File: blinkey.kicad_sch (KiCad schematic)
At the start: 34 parts, among them SW1 SW_DIP_x04

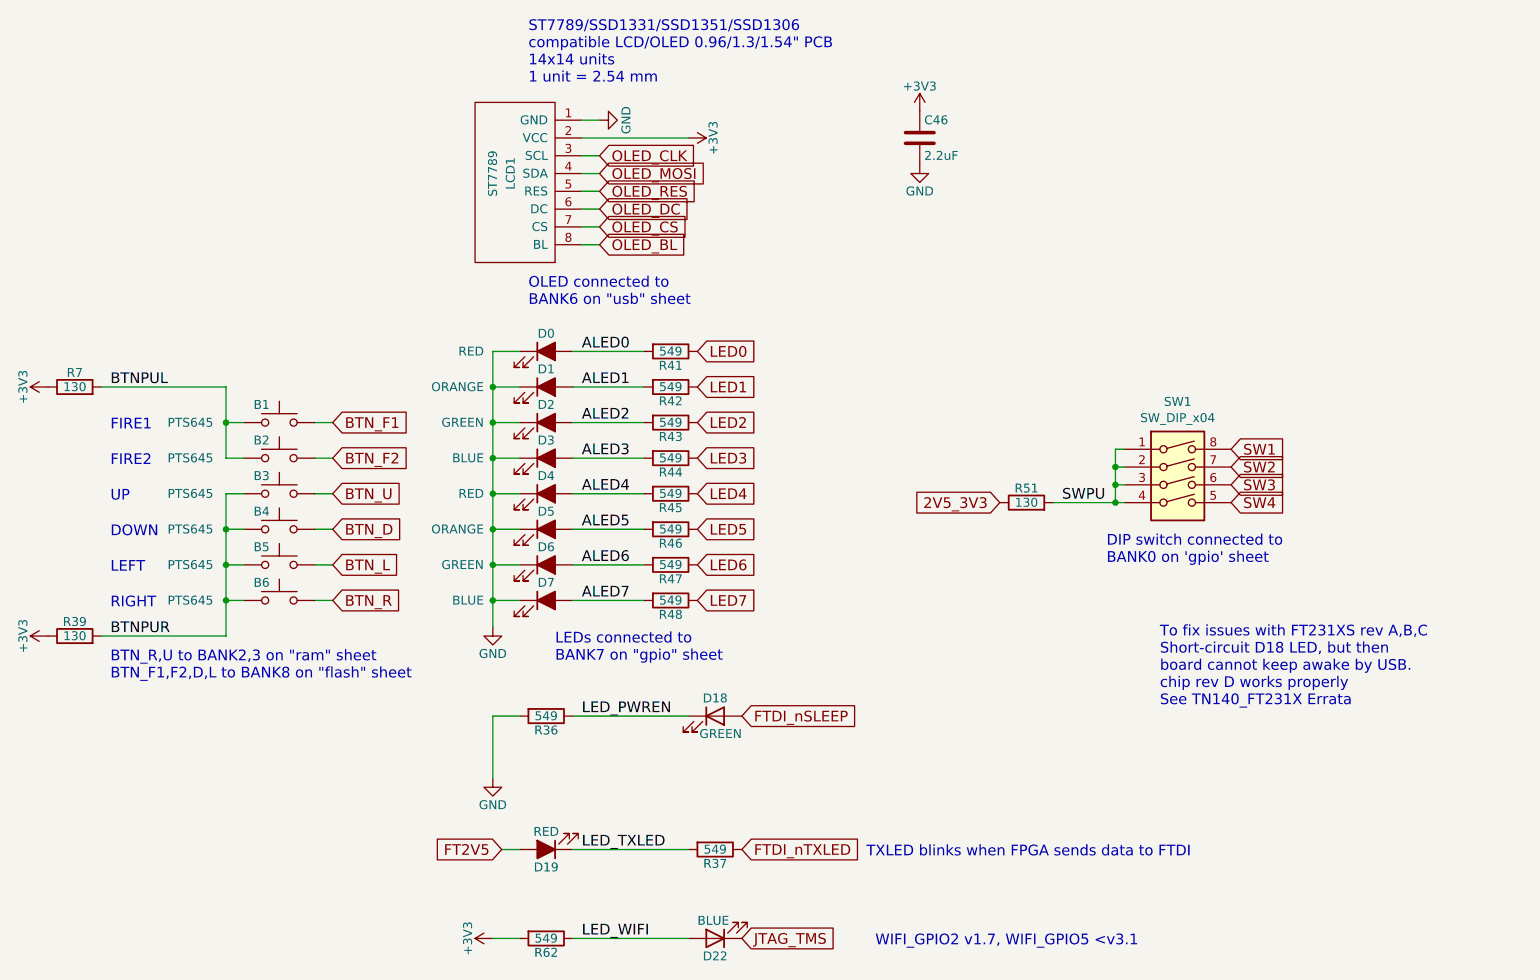
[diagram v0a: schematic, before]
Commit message: remove unneeded components from schema
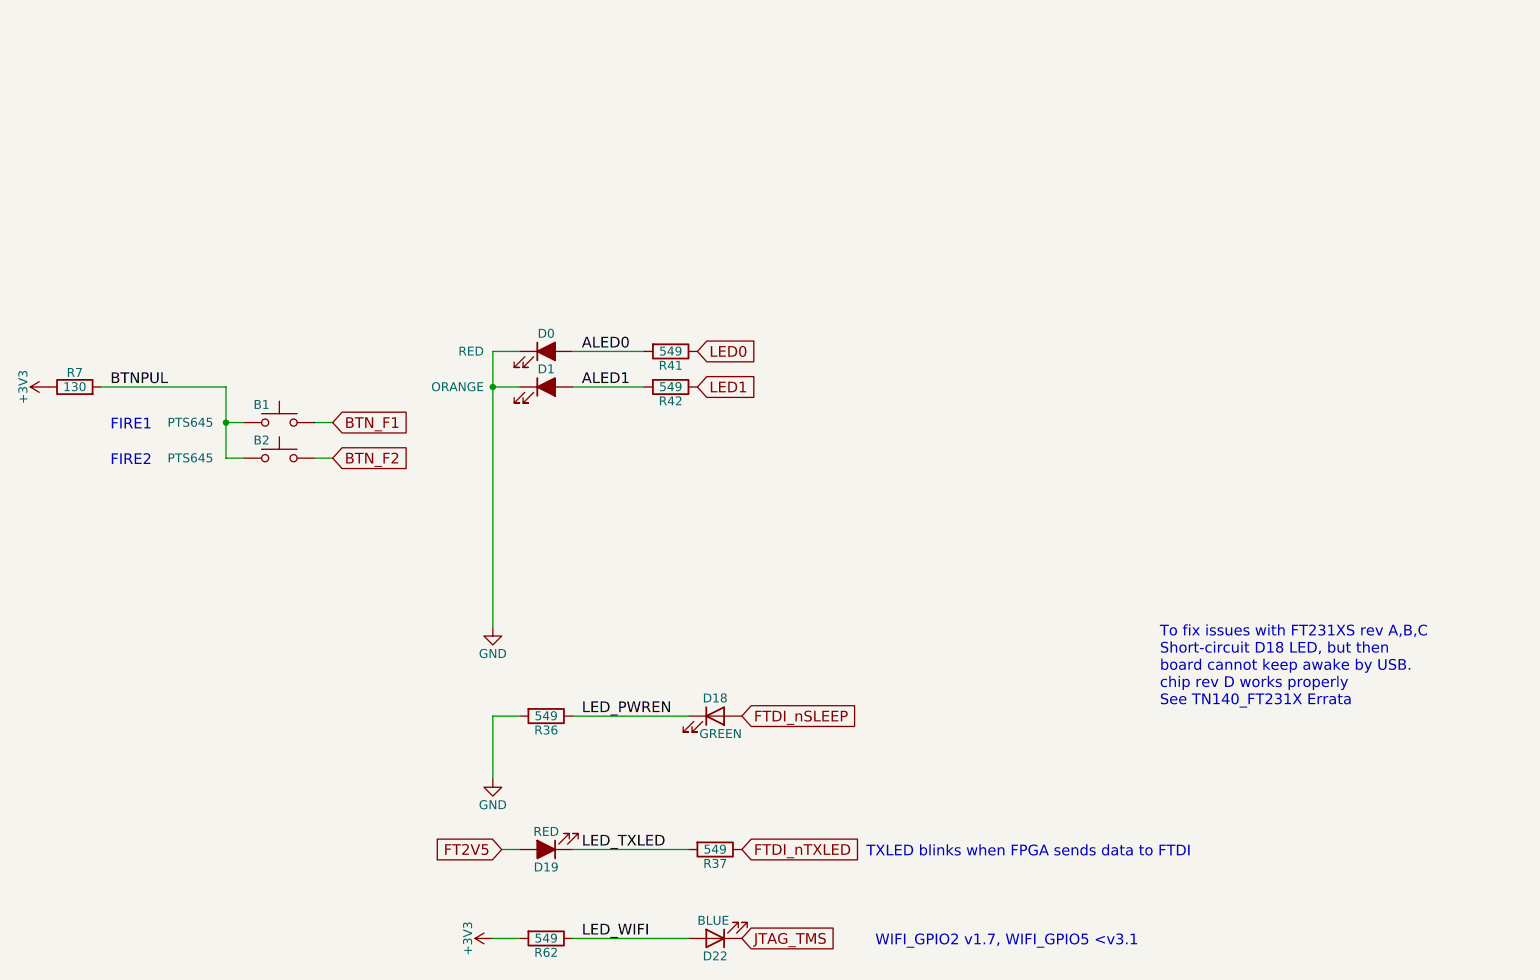
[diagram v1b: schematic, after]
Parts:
- removed B3, B4, B5, B6: PTS645, Button_Switch_SMD:SW_SPST_PTS645, symbol Switch:SW_Push
- removed C46: 2.2uF, Capacitor_SMD:C_0805_2012Metric, symbol Device:C
- removed D2, D6: GREEN, LED_SMD:LED_0805_2012Metric, symbol Device:LED_ALT
- removed D3, D7: BLUE, LED_SMD:LED_0805_2012Metric, symbol Device:LED_ALT
- removed D4: RED, LED_SMD:LED_0805_2012Metric, symbol Device:LED_ALT
- removed D5: ORANGE, LED_SMD:LED_0805_2012Metric, symbol Device:LED_ALT
- removed LCD1: ST7789, st7789:st7789, symbol st7789:ST7789
- removed R39, R51: 130, Resistor_SMD:R_0603_1608Metric, symbol Device:R
- removed R43, R44, R45, R46, R47, R48: 549, Resistor_SMD:R_0603_1608Metric, symbol Device:R
- removed SW1: SW_DIP_x04, dipswitch:SW_DIP_x4_W8.61mm_Slide_LowProfile, symbol Switch:SW_DIP_x04
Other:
- note removed: "BTN_R,U to BANK2,3 on "ram" sheet BTN_F1,F2,D,L to BANK8 on "flash" sheet"
- note removed: "DIP switch connected to BANK0 on 'gpio' sheet"
- note removed: "DOWN"
- note removed: "LEDs connected to BANK7 on "gpio" sheet"
- note removed: "LEFT"
- note removed: "OLED connected to BANK6 on "usb" sheet"
- note removed: "RIGHT"
- note removed: "ST7789/SSD1331/SSD1351/SSD1306 compatible LCD/OLED 0.96/1.3/1.54" PCB 14x14 units 1 unit = 2.54 mm"
- note removed: "UP"

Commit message: start to normalize bom
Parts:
- B1, B2: Digikey (none) -> CKN9088CT-ND; LCSC (none) -> C285463
- D19: Digikey (none) -> 160-1415-1-ND; LCSC (none) -> C94868
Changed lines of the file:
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@@
+			)
+		)
+		(property "LCSC" "C285463"
+			(at 77.47 74.93 0)
+			(effects
+				(font
+					(size 1.27 1.27)
+				)
+				(hide yes)
+			)
+		)
+		(property "Digikey" "CKN9088CT-ND"
+			(at 77.47 74.93 0)
+			(effects
+				(font
+					(size 1.27 1.27)
+				)
+				(hide yes)
 			)
 		)
@@
 			)
 		)
+		(property "LCSC" "C94868"
+			(at 115.57 135.89 0)
+			(effects
+				(font
+					(size 1.27 1.27)
+				)
+				(hide yes)
+			)
+		)
+		(property "Digikey" "160-1415-1-ND"
+			(at 115.57 135.89 0)
+			(effects
+				(font
+					(size 1.27 1.27)
+				)
+				(hide yes)
+			)
+		)
 		(pin "1"
 		)
@@
 				)
 				(hide yes)
+			)
+		)
+		(property "LCSC" "C285463"
+			(at 77.47 80.01 0)
+			(effects
+				(font
+					(size 1.27 1.27)
+				)
+				(hide yes)
+			)
+		)
+		(property "Digikey" "CKN9088CT-ND"
+			(at 77.47 80.01 0)
+			(effects
+				(font
+					(size 1.27 1.27)
+				)
+				(hide yes)

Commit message: updating part numbers across schematcs
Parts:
- R36, R37, R41, R42, R62: Digikey (none) -> 13-AC0603FR-07549RLCT-ND; MPN (none) -> 13-AC0603FR-07549RLCT-ND
- R7: Digikey (none) -> 13-AC0603FR-07130RLCT-ND; MPN (none) -> 13-AC0603FR-07130RLCT-ND
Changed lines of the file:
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@@
+			)
+		)
+		(property "Digikey" "13-AC0603FR-07130RLCT-ND"
+			(at 48.26 69.85 90)
+			(effects
+				(font
+					(size 1.27 1.27)
+				)
+				(hide yes)
+			)
+		)
+		(property "MPN" "13-AC0603FR-07130RLCT-ND"
+			(at 48.26 69.85 90)
+			(effects
+				(font
+					(size 1.27 1.27)
+				)
+				(hide yes)
 			)
 		)
@@
 			)
 		)
+		(property "Digikey" "13-AC0603FR-07549RLCT-ND"
+			(at 115.57 116.84 90)
+			(effects
+				(font
+					(size 1.27 1.27)
+				)
+				(hide yes)
+			)
+		)
+		(property "MPN" "13-AC0603FR-07549RLCT-ND"
+			(at 115.57 116.84 90)
+			(effects
+				(font
+					(size 1.27 1.27)
+				)
+				(hide yes)
+			)
+		)
 		(pin "1"
 		)
@@
 			)
 		)
+		(property "Digikey" "13-AC0603FR-07549RLCT-ND"
+			(at 139.7 135.89 90)
+			(effects
+				(font
+					(size 1.27 1.27)
+				)
+				(hide yes)
+			)
+		)
+		(property "MPN" "13-AC0603FR-07549RLCT-ND"
+			(at 139.7 135.89 90)
+			(effects
+				(font
+					(size 1.27 1.27)
+				)
+				(hide yes)
+			)
+		)
 		(pin "1"
 		)
@@
 			)
 		)
+		(property "Digikey" "13-AC0603FR-07549RLCT-ND"
+			(at 133.35 64.77 90)
+			(effects
+				(font
+					(size 1.27 1.27)
+				)
+				(hide yes)
+			)
+		)
+		(property "MPN" "13-AC0603FR-07549RLCT-ND"
+			(at 133.35 64.77 90)
+			(effects
+				(font
+					(size 1.27 1.27)
+				)
+				(hide yes)
+			)
+		)
 		(pin "1"
 		)
@@
 			)
 		)
+		(property "Digikey" "13-AC0603FR-07549RLCT-ND"
+			(at 133.35 69.85 90)
+			(effects
+				(font
+					(size 1.27 1.27)
+				)
+				(hide yes)
+			)
+		)
+		(property "MPN" "13-AC0603FR-07549RLCT-ND"
+			(at 133.35 69.85 90)
+			(effects
+				(font
+					(size 1.27 1.27)
+				)
+				(hide yes)
+			)
+		)
 		(pin "1"
 		)
@@
 			)
 		)
+		(property "Digikey" "13-AC0603FR-07549RLCT-ND"
+			(at 115.57 148.59 90)
+			(effects
+				(font
+					(size 1.27 1.27)
+				)
+				(hide yes)
+			)
+		)
+		(property "MPN" "13-AC0603FR-07549RLCT-ND"
+			(at 115.57 148.59 90)
+			(effects
+				(font
+					(size 1.27 1.27)
+				)
+				(hide yes)
+			)
+		)

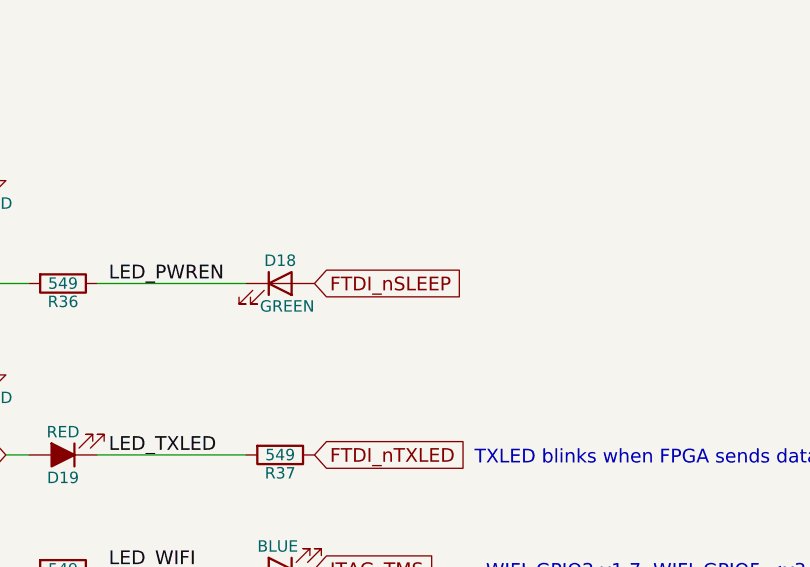
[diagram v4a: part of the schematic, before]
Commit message: remove wake up/shutdown logic
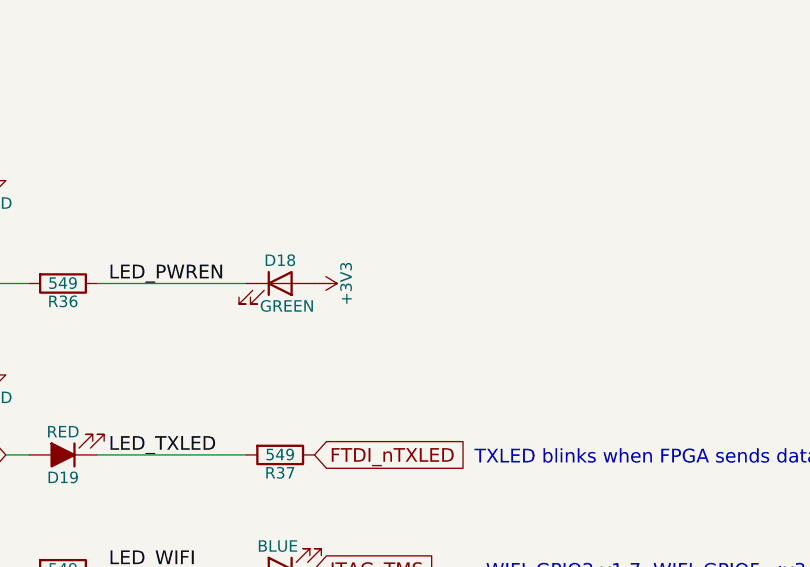
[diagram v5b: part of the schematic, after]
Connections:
- net FTDI_nSLEEP is gone; now on net +3V3: D18.2 (A)
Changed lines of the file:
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@@
-		)
-	)
-	(global_label "FTDI_nSLEEP"
-		(shape input)
-		(at 143.51 116.84 0)
-		(effects
-			(font
-				(size 1.524 1.524)
-			)
-			(justify left)
-		)
-		(property "Intersheetrefs" "${INTERSHEET_REFS}"
-			(at 143.51 116.84 0)
-			(hide yes)
-			(show_name no)
-			(do_not_autoplace no)
-			(effects
-				(font
-					(size 1.27 1.27)
-				)
-			)
 		)
 	)
@@
 					(unit 1)
 				)
+			)
+		)
+	)
+	(symbol
+		(lib_id "power:+3V3")
+		(at 143.51 116.84 270)
+		(unit 1)
+		(body_style 1)
+		(exclude_from_sim no)
+		(in_bom yes)
+		(on_board yes)
+		(in_pos_files yes)
+		(dnp no)
+		(property "Reference" "#PWR082"
+			(at 139.7 116.84 0)
+			(hide yes)
+			(show_name no)
+			(do_not_autoplace no)
+			(effects
+				(font
+					(size 1.27 1.27)
+				)
+			)
+		)
+		(property "Value" "+3V3"
+			(at 147.066 116.84 0)
+			(show_name no)
+			(do_not_autoplace no)
+			(effects
+				(font
+					(size 1.27 1.27)
+				)
+			)
+		)
+		(property "Footprint" ""
+			(at 143.51 116.84 0)
+			(show_name no)
+			(do_not_autoplace no)
+			(effects
+				(font
+					(size 1.27 1.27)
+				)
+			)
+		)
+		(property "Datasheet" ""
+			(at 143.51 116.84 0)
+			(show_name no)
+			(do_not_autoplace no)
+			(effects
+				(font
+					(size 1.27 1.27)
+				)
+			)
+		)
+		(property "Description" ""
+			(at 143.51 116.84 0)
+			(show_name no)
+			(do_not_autoplace no)
+			(effects
+				(font
+					(size 1.27 1.27)
+				)
+			)
+		)
+		(pin "1"
+		)
+		(instances
+			(project "ulx3s"
+				(path "/49a43414-f3c1-43b2-ad20-ac3166075f21/00000000-0000-0000-0000-000058d6547c"
+					(reference "#PWR082")
+					(unit 1)
+				)

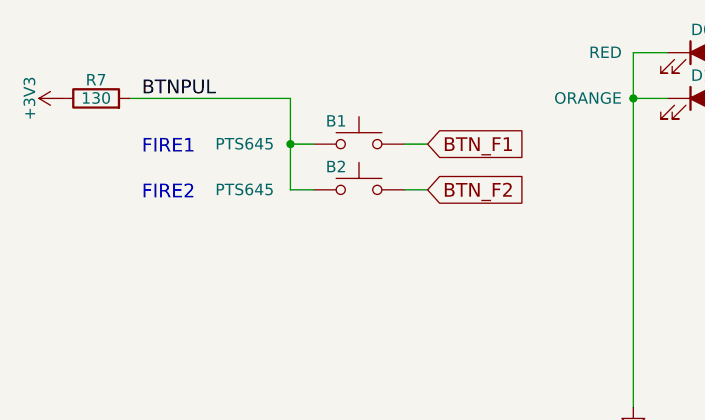
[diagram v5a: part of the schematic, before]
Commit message: remove buttons f1/f2
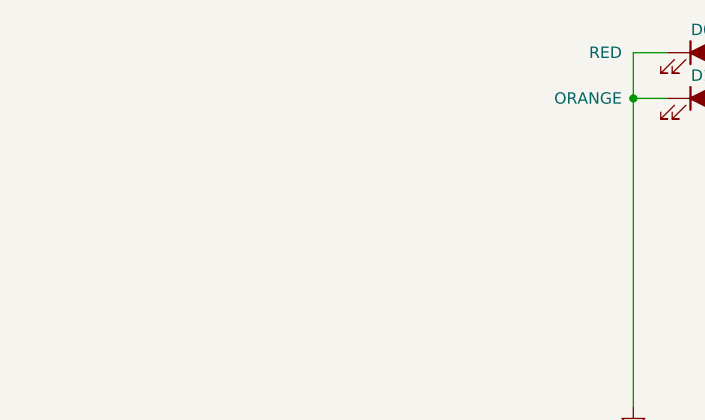
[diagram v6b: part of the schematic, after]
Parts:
- removed B1, B2: PTS645, Button_Switch_SMD:SW_SPST_PTS645, symbol Switch:SW_Push
- removed R7: 130, Resistor_SMD:R_0603_1608Metric, symbol Device:R
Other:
- note removed: "FIRE1"
- note removed: "FIRE2"
